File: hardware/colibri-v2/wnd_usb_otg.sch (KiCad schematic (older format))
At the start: 15 parts

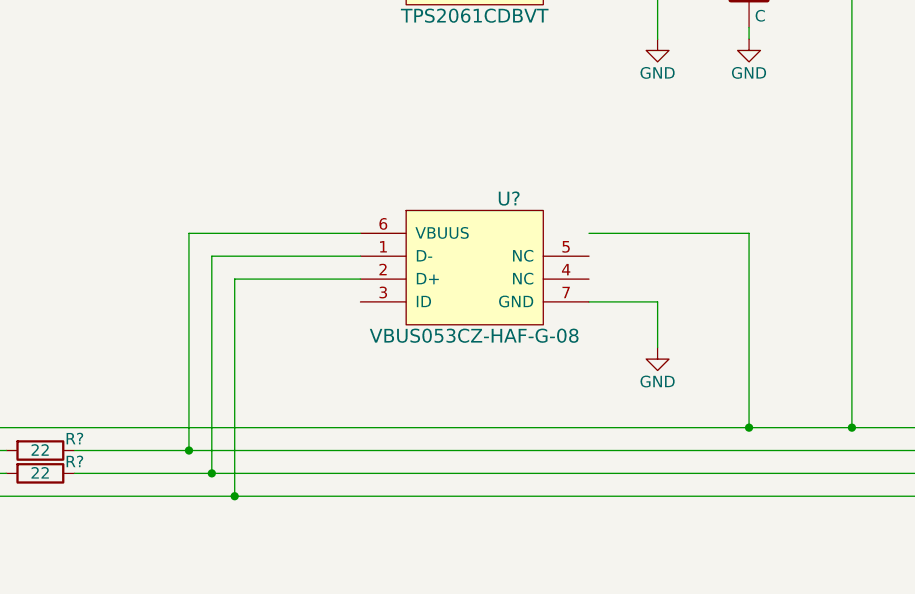
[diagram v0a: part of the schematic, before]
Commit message: Added Wandboard USB Host
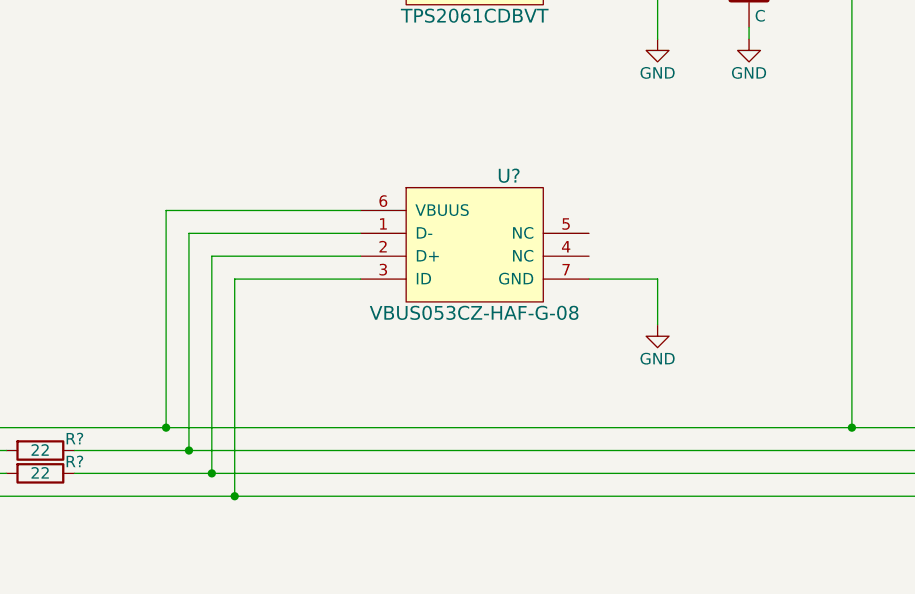
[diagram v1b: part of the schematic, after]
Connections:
- net OTG_FS_ID: now also U?.3 (ID); no longer U?.2 (D+)
- net VBUS_FS: now also U?.6 (VBUUS)
- net at P?.2 (D-), R?.1: now also U?.1 (D-); no longer U?.6 (VBUUS)
- net at P?.3 (D+), R?.1: now also U?.2 (D+); no longer U?.1 (D-)
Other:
- moved on the sheet: U?
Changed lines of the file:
@@
 $Descr A4 11693 8268
 encoding utf-8
-Sheet 13 21
+Sheet 13 22
 Title ""
 Date ""
@@
 L VBUS053CZ-HAF-G-08 U?
 U 1 1 5614C949
-P 4300 3850
-F 0 "U?" H 4450 4150 60  0000 C CNN
-F 1 "VBUS053CZ-HAF-G-08" H 4300 3550 60  0000 C CNN
-F 2 "" H 4250 4550 60  0000 C CNN
-F 3 "" H 4250 4550 60  0000 C CNN
-	1    4300 3850
+P 4300 3750
+F 0 "U?" H 4450 4050 60  0000 C CNN
+F 1 "VBUS053CZ-HAF-G-08" H 4300 3450 60  0000 C CNN
+F 2 "" H 4250 4450 60  0000 C CNN
+F 3 "" H 4250 4450 60  0000 C CNN
+	1    4300 3750
 	1    0    0    -1
 $EndComp
@@
 L GND #PWR?
 U 1 1 5614C9CE
-P 5100 4200
-F 0 "#PWR?" H 5100 3950 50  0001 C CNN
-F 1 "GND" H 5100 4050 50  0000 C CNN
-F 2 "" H 5100 4200 60  0000 C CNN
-F 3 "" H 5100 4200 60  0000 C CNN
-	1    5100 4200
+P 5100 4100
+F 0 "#PWR?" H 5100 3850 50  0001 C CNN
+F 1 "GND" H 5100 3950 50  0000 C CNN
+F 2 "" H 5100 4100 60  0000 C CNN
+F 3 "" H 5100 4100 60  0000 C CNN
+	1    5100 4100
 	1    0    0    -1
 $EndComp
@@
 Connection ~ 8100 2700
 Wire Wire Line
-	4800 4000 5100 4000
-Wire Wire Line
-	5100 4000 5100 4200
-Wire Wire Line
-	4800 3700 5500 3700
-Wire Wire Line
-	5500 3700 5500 4550
-Connection ~ 5500 4550
+	4800 3900 5100 3900
+Wire Wire Line
+	5100 3900 5100 4100
 Wire Wire Line
 	3800 3900 3250 3900
@@
 Wire Wire Line
 	5100 2600 5100 2850
+Wire Wire Line
+	3800 3600 2950 3600
+Wire Wire Line
+	2950 3600 2950 4550
+Connection ~ 2950 4550
 $EndSCHEMATC

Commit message: Annotated Components
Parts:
- gave numbers to parts that had none: 15
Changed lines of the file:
@@
 $EndDescr
 $Comp
-L USB_OTG P?
+L USB_OTG P8
 U 1 1 5614C935
 P 8300 4750
-F 0 "P?" H 8625 4625 50  0000 C CNN
+F 0 "P8" H 8625 4625 50  0000 C CNN
 F 1 "USB_OTG" H 8300 4950 50  0000 C CNN
 F 2 "" V 8250 4650 60  0000 C CNN
@@
 OTG_FS_PSO
 $Comp
-L VBUS053CZ-HAF-G-08 U?
+L VBUS053CZ-HAF-G-08 U10
 U 1 1 5614C949
 P 4300 3750
-F 0 "U?" H 4450 4050 60  0000 C CNN
+F 0 "U10" H 4450 4050 60  0000 C CNN
 F 1 "VBUS053CZ-HAF-G-08" H 4300 3450 60  0000 C CNN
 F 2 "" H 4250 4450 60  0000 C CNN
@@
 $EndComp
 $Comp
-L R R?
+L R R60
 U 1 1 5614C950
 P 2400 4650
-F 0 "R?" V 2350 4800 50  0000 C CNN
+F 0 "R60" V 2350 4800 50  0000 C CNN
 F 1 "22" V 2400 4650 50  0000 C CNN
 F 2 "" V 2330 4650 30  0000 C CNN
@@
 $EndComp
 $Comp
-L R R?
+L R R61
 U 1 1 5614C957
 P 2400 4750
-F 0 "R?" V 2350 4900 50  0000 C CNN
+F 0 "R61" V 2350 4900 50  0000 C CNN
 F 1 "22" V 2400 4750 50  0000 C CNN
 F 2 "" V 2330 4750 30  0000 C CNN
@@
 $EndComp
 $Comp
-L +3V3 #PWR?
+L +3V3 #PWR88
 U 1 1 5614C95E
 P 2100 1400
-F 0 "#PWR?" H 2100 1250 50  0001 C CNN
+F 0 "#PWR88" H 2100 1250 50  0001 C CNN
 F 1 "+3V3" H 2100 1540 50  0000 C CNN
 F 2 "" H 2100 1400 60  0000 C CNN
@@
 $EndComp
 $Comp
-L R R?
+L R R59
 U 1 1 5614C964
 P 2100 1950
-F 0 "R?" V 2180 1950 50  0000 C CNN
+F 0 "R59" V 2180 1950 50  0000 C CNN
 F 1 "10K" V 2100 1950 50  0000 C CNN
 F 2 "" V 2030 1950 30  0000 C CNN
@@
 $EndComp
 $Comp
-L +3V3 #PWR?
+L +3V3 #PWR89
 U 1 1 5614C96B
 P 2450 1400
-F 0 "#PWR?" H 2450 1250 50  0001 C CNN
+F 0 "#PWR89" H 2450 1250 50  0001 C CNN
 F 1 "+3V3" H 2450 1540 50  0000 C CNN
 F 2 "" H 2450 1400 60  0000 C CNN
@@
 $EndComp
 $Comp
-L R R?
+L R R62
 U 1 1 5614C971
 P 2450 1950
-F 0 "R?" V 2530 1950 50  0000 C CNN
+F 0 "R62" V 2530 1950 50  0000 C CNN
 F 1 "47K" V 2450 1950 50  0000 C CNN
 F 2 "" V 2380 1950 30  0000 C CNN
@@
 $EndComp
 $Comp
-L LED D?
+L LED D13
 U 1 1 5614C978
 P 2800 2100
-F 0 "D?" H 2800 2200 50  0000 C CNN
+F 0 "D13" H 2800 2200 50  0000 C CNN
 F 1 "RED" H 2800 2000 50  0000 C CNN
 F 2 "" H 2800 2100 60  0000 C CNN
@@
 $EndComp
 $Comp
-L R R?
+L R R63
 U 1 1 5614C97F
 P 2800 1650
-F 0 "R?" V 2880 1650 50  0000 C CNN
+F 0 "R63" V 2880 1650 50  0000 C CNN
 F 1 "620" V 2800 1650 50  0000 C CNN
 F 2 "" V 2730 1650 30  0000 C CNN
@@
 $EndComp
 $Comp
-L +3V3 #PWR?
+L +3V3 #PWR90
 U 1 1 5614C986
 P 2800 1400
-F 0 "#PWR?" H 2800 1250 50  0001 C CNN
+F 0 "#PWR90" H 2800 1250 50  0001 C CNN
 F 1 "+3V3" H 2800 1540 50  0000 C CNN
 F 2 "" H 2800 1400 60  0000 C CNN
@@
 $EndComp
 $Comp
-L LED D?
+L LED D14
 U 1 1 5614C98C
 P 8100 1850
-F 0 "D?" H 8100 1950 50  0000 C CNN
+F 0 "D14" H 8100 1950 50  0000 C CNN
 F 1 "GREEN" H 8100 1750 50  0000 C CNN
 F 2 "" H 8100 1850 60  0000 C CNN
@@
 $EndComp
 $Comp
-L R R?
+L R R66
 U 1 1 5614C993
 P 8100 1450
-F 0 "R?" V 8180 1450 50  0000 C CNN
+F 0 "R66" V 8180 1450 50  0000 C CNN
 F 1 "620" V 8100 1450 50  0000 C CNN
 F 2 "" V 8030 1450 30  0000 C CNN
@@
 $EndComp
 $Comp
-L +3V3 #PWR?
+L +3V3 #PWR96
 U 1 1 5614C99A
 P 8100 1200
-F 0 "#PWR?" H 8100 1050 50  0001 C CNN
+F 0 "#PWR96" H 8100 1050 50  0001 C CNN
 F 1 "+3V3" H 8100 1340 50  0000 C CNN
 F 2 "" H 8100 1200 60  0000 C CNN
@@
 $EndComp
 $Comp
-L Q_NMOS_GSD Q?
+L Q_NMOS_GSD Q7
 U 1 1 5614C9A0
 P 8000 2400
-F 0 "Q?" H 8300 2450 50  0000 R CNN
+F 0 "Q7" H 8300 2450 50  0000 R CNN
 F 1 "BSS138PW" H 8650 2350 50  0000 R CNN
 F 2 "" H 8200 2500 29  0000 C CNN
@@
 $EndComp
 $Comp
-L GND #PWR?
+L GND #PWR97
 U 1 1 5614C9A7
 P 8100 2850
-F 0 "#PWR?" H 8100 2600 50  0001 C CNN
+F 0 "#PWR97" H 8100 2600 50  0001 C CNN
 F 1 "GND" H 8100 2700 50  0000 C CNN
 F 2 "" H 8100 2850 60  0000 C CNN
@@
 $EndComp
 $Comp
-L R R?
+L R R64
 U 1 1 5614C9AD
 P 7300 2400
-F 0 "R?" V 7380 2400 50  0000 C CNN
+F 0 "R64" V 7380 2400 50  0000 C CNN
 F 1 "10K" V 7300 2400 50  0000 C CNN
 F 2 "" V 7230 2400 30  0000 C CNN
@@
 $EndComp
 $Comp
-L R R?
+L R R65
 U 1 1 5614C9B4
 P 7850 2700
-F 0 "R?" V 7930 2700 50  0000 C CNN
+F 0 "R65" V 7930 2700 50  0000 C CNN
 F 1 "47K" V 7850 2700 50  0000 C CNN
 F 2 "" V 7780 2700 30  0000 C CNN
@@
 $EndComp
 $Comp
-L C C?
+L C C64
 U 1 1 5614C9BB
 P 5500 2650
-F 0 "C?" H 5525 2750 50  0000 L CNN
+F 0 "C64" H 5525 2750 50  0000 L CNN
 F 1 "C" H 5525 2550 50  0000 L CNN
 F 2 "" H 5538 2500 30  0000 C CNN
@@
 $EndComp
 $Comp
-L GND #PWR?
+L GND #PWR94
 U 1 1 5614C9C2
 P 5500 2850
-F 0 "#PWR?" H 5500 2600 50  0001 C CNN
+F 0 "#PWR94" H 5500 2600 50  0001 C CNN
 F 1 "GND" H 5500 2700 50  0000 C CNN
 F 2 "" H 5500 2850 60  0000 C CNN
@@
 $EndComp
 $Comp
-L GND #PWR?
+L GND #PWR92
 U 1 1 5614C9C8
 P 5100 2850
-F 0 "#PWR?" H 5100 2600 50  0001 C CNN
+F 0 "#PWR92" H 5100 2600 50  0001 C CNN
 F 1 "GND" H 5100 2700 50  0000 C CNN
 F 2 "" H 5100 2850 60  0000 C CNN
@@
 $EndComp
 $Comp
-L GND #PWR?
+L GND #PWR93
 U 1 1 5614C9CE
 P 5100 4100
-F 0 "#PWR?" H 5100 3850 50  0001 C CNN
+F 0 "#PWR93" H 5100 3850 50  0001 C CNN
 F 1 "GND" H 5100 3950 50  0000 C CNN
 F 2 "" H 5100 4100 60  0000 C CNN
@@
 Connection ~ 3050 4650
 $Comp
-L GND #PWR?
+L GND #PWR95
 U 1 1 5614CA07
 P 7900 5400
-F 0 "#PWR?" H 7900 5150 50  0001 C CNN
+F 0 "#PWR95" H 7900 5150 50  0001 C CNN
 F 1 "GND" H 7900 5250 50  0000 C CNN
 F 2 "" H 7900 5400 60  0000 C CNN
@@
 Connection ~ 7900 5300
 $Comp
-L +5V #PWR?
+L +5V #PWR91
 U 1 1 5614CA12
 P 3150 1400
-F 0 "#PWR?" H 3150 1250 50  0001 C CNN
+F 0 "#PWR91" H 3150 1250 50  0001 C CNN
 F 1 "+5V" H 3150 1540 50  0000 C CNN
 F 2 "" H 3150 1400 60  0000 C CNN
@@
 $EndComp
 $Comp
-L TPS2061CDBVT U?
+L TPS2061CDBVT U9
 U 1 1 5614D158
 P 4300 2500
-F 0 "U?" H 4550 2750 60  0000 C CNN
+F 0 "U9" H 4550 2750 60  0000 C CNN
 F 1 "TPS2061CDBVT" H 4300 2250 60  0000 C CNN
 F 2 "" H 4300 2300 60  0000 C CNN

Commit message: Re-annotated schematic
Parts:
- renumbered C64 to C62, R59 to R60, R60 to R61, R61 to R62, R62 to R63, R63 to R64, R64 to R65, R65 to R66, R66 to R67
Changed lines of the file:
@@
 $EndComp
 $Comp
-L R R60
+L R R61
 U 1 1 5614C950
 P 2400 4650
-F 0 "R60" V 2350 4800 50  0000 C CNN
+F 0 "R61" V 2350 4800 50  0000 C CNN
 F 1 "22" V 2400 4650 50  0000 C CNN
 F 2 "" V 2330 4650 30  0000 C CNN
@@
 $EndComp
 $Comp
-L R R61
+L R R62
 U 1 1 5614C957
 P 2400 4750
-F 0 "R61" V 2350 4900 50  0000 C CNN
+F 0 "R62" V 2350 4900 50  0000 C CNN
 F 1 "22" V 2400 4750 50  0000 C CNN
 F 2 "" V 2330 4750 30  0000 C CNN
@@
 $EndComp
 $Comp
-L +3V3 #PWR090
+L +3V3 #PWR85
 U 1 1 5614C95E
 P 2100 1400
-F 0 "#PWR090" H 2100 1250 50  0001 C CNN
+F 0 "#PWR85" H 2100 1250 50  0001 C CNN
 F 1 "+3V3" H 2100 1540 50  0000 C CNN
 F 2 "" H 2100 1400 60  0000 C CNN
@@
 $EndComp
 $Comp
-L R R59
+L R R60
 U 1 1 5614C964
 P 2100 1950
-F 0 "R59" V 2180 1950 50  0000 C CNN
+F 0 "R60" V 2180 1950 50  0000 C CNN
 F 1 "10K" V 2100 1950 50  0000 C CNN
 F 2 "" V 2030 1950 30  0000 C CNN
@@
 $EndComp
 $Comp
-L +3V3 #PWR091
+L +3V3 #PWR86
 U 1 1 5614C96B
 P 2450 1400
-F 0 "#PWR091" H 2450 1250 50  0001 C CNN
+F 0 "#PWR86" H 2450 1250 50  0001 C CNN
 F 1 "+3V3" H 2450 1540 50  0000 C CNN
 F 2 "" H 2450 1400 60  0000 C CNN
@@
 $EndComp
 $Comp
-L R R62
+L R R63
 U 1 1 5614C971
 P 2450 1950
-F 0 "R62" V 2530 1950 50  0000 C CNN
+F 0 "R63" V 2530 1950 50  0000 C CNN
 F 1 "47K" V 2450 1950 50  0000 C CNN
 F 2 "" V 2380 1950 30  0000 C CNN
@@
 $EndComp
 $Comp
-L R R63
+L R R64
 U 1 1 5614C97F
 P 2800 1650
-F 0 "R63" V 2880 1650 50  0000 C CNN
+F 0 "R64" V 2880 1650 50  0000 C CNN
 F 1 "620" V 2800 1650 50  0000 C CNN
 F 2 "" V 2730 1650 30  0000 C CNN
@@
 $EndComp
 $Comp
-L +3V3 #PWR092
+L +3V3 #PWR87
 U 1 1 5614C986
 P 2800 1400
-F 0 "#PWR092" H 2800 1250 50  0001 C CNN
+F 0 "#PWR87" H 2800 1250 50  0001 C CNN
 F 1 "+3V3" H 2800 1540 50  0000 C CNN
 F 2 "" H 2800 1400 60  0000 C CNN
@@
 $EndComp
 $Comp
-L R R66
+L R R67
 U 1 1 5614C993
 P 8100 1450
-F 0 "R66" V 8180 1450 50  0000 C CNN
+F 0 "R67" V 8180 1450 50  0000 C CNN
 F 1 "620" V 8100 1450 50  0000 C CNN
 F 2 "" V 8030 1450 30  0000 C CNN
@@
 $EndComp
 $Comp
-L +3V3 #PWR093
+L +3V3 #PWR93
 U 1 1 5614C99A
 P 8100 1200
-F 0 "#PWR093" H 8100 1050 50  0001 C CNN
+F 0 "#PWR93" H 8100 1050 50  0001 C CNN
 F 1 "+3V3" H 8100 1340 50  0000 C CNN
 F 2 "" H 8100 1200 60  0000 C CNN
@@
 $EndComp
 $Comp
-L GND #PWR094
+L GND #PWR94
 U 1 1 5614C9A7
 P 8100 2850
-F 0 "#PWR094" H 8100 2600 50  0001 C CNN
+F 0 "#PWR94" H 8100 2600 50  0001 C CNN
 F 1 "GND" H 8100 2700 50  0000 C CNN
 F 2 "" H 8100 2850 60  0000 C CNN
@@
 $EndComp
 $Comp
-L R R64
+L R R65
 U 1 1 5614C9AD
 P 7300 2400
-F 0 "R64" V 7380 2400 50  0000 C CNN
+F 0 "R65" V 7380 2400 50  0000 C CNN
 F 1 "10K" V 7300 2400 50  0000 C CNN
 F 2 "" V 7230 2400 30  0000 C CNN
@@
 $EndComp
 $Comp
-L R R65
+L R R66
 U 1 1 5614C9B4
 P 7850 2700
-F 0 "R65" V 7930 2700 50  0000 C CNN
+F 0 "R66" V 7930 2700 50  0000 C CNN
 F 1 "47K" V 7850 2700 50  0000 C CNN
 F 2 "" V 7780 2700 30  0000 C CNN
@@
 $EndComp
 $Comp
-L C C64
+L C C62
 U 1 1 5614C9BB
 P 5500 2650
-F 0 "C64" H 5525 2750 50  0000 L CNN
+F 0 "C62" H 5525 2750 50  0000 L CNN
 F 1 "C" H 5525 2550 50  0000 L CNN
 F 2 "" H 5538 2500 30  0000 C CNN
@@
 $EndComp
 $Comp
-L GND #PWR095
+L GND #PWR91
 U 1 1 5614C9C2
 P 5500 2850
-F 0 "#PWR095" H 5500 2600 50  0001 C CNN
+F 0 "#PWR91" H 5500 2600 50  0001 C CNN
 F 1 "GND" H 5500 2700 50  0000 C CNN
 F 2 "" H 5500 2850 60  0000 C CNN
@@
 $EndComp
 $Comp
-L GND #PWR096
+L GND #PWR89
 U 1 1 5614C9C8
 P 5100 2850
-F 0 "#PWR096" H 5100 2600 50  0001 C CNN
+F 0 "#PWR89" H 5100 2600 50  0001 C CNN
 F 1 "GND" H 5100 2700 50  0000 C CNN
 F 2 "" H 5100 2850 60  0000 C CNN
@@
 $EndComp
 $Comp
-L GND #PWR097
+L GND #PWR90
 U 1 1 5614C9CE
 P 5100 4100
-F 0 "#PWR097" H 5100 3850 50  0001 C CNN
+F 0 "#PWR90" H 5100 3850 50  0001 C CNN
 F 1 "GND" H 5100 3950 50  0000 C CNN
 F 2 "" H 5100 4100 60  0000 C CNN
@@
 Connection ~ 3050 4650
 $Comp
-L GND #PWR098
+L GND #PWR92
 U 1 1 5614CA07
 P 7900 5400
-F 0 "#PWR098" H 7900 5150 50  0001 C CNN
+F 0 "#PWR92" H 7900 5150 50  0001 C CNN
 F 1 "GND" H 7900 5250 50  0000 C CNN
 F 2 "" H 7900 5400 60  0000 C CNN
@@
 Connection ~ 7900 5300
 $Comp
-L +5V #PWR099
+L +5V #PWR88
 U 1 1 5614CA12
 P 3150 1400
-F 0 "#PWR099" H 3150 1250 50  0001 C CNN
+F 0 "#PWR88" H 3150 1250 50  0001 C CNN
 F 1 "+5V" H 3150 1540 50  0000 C CNN
 F 2 "" H 3150 1400 60  0000 C CNN

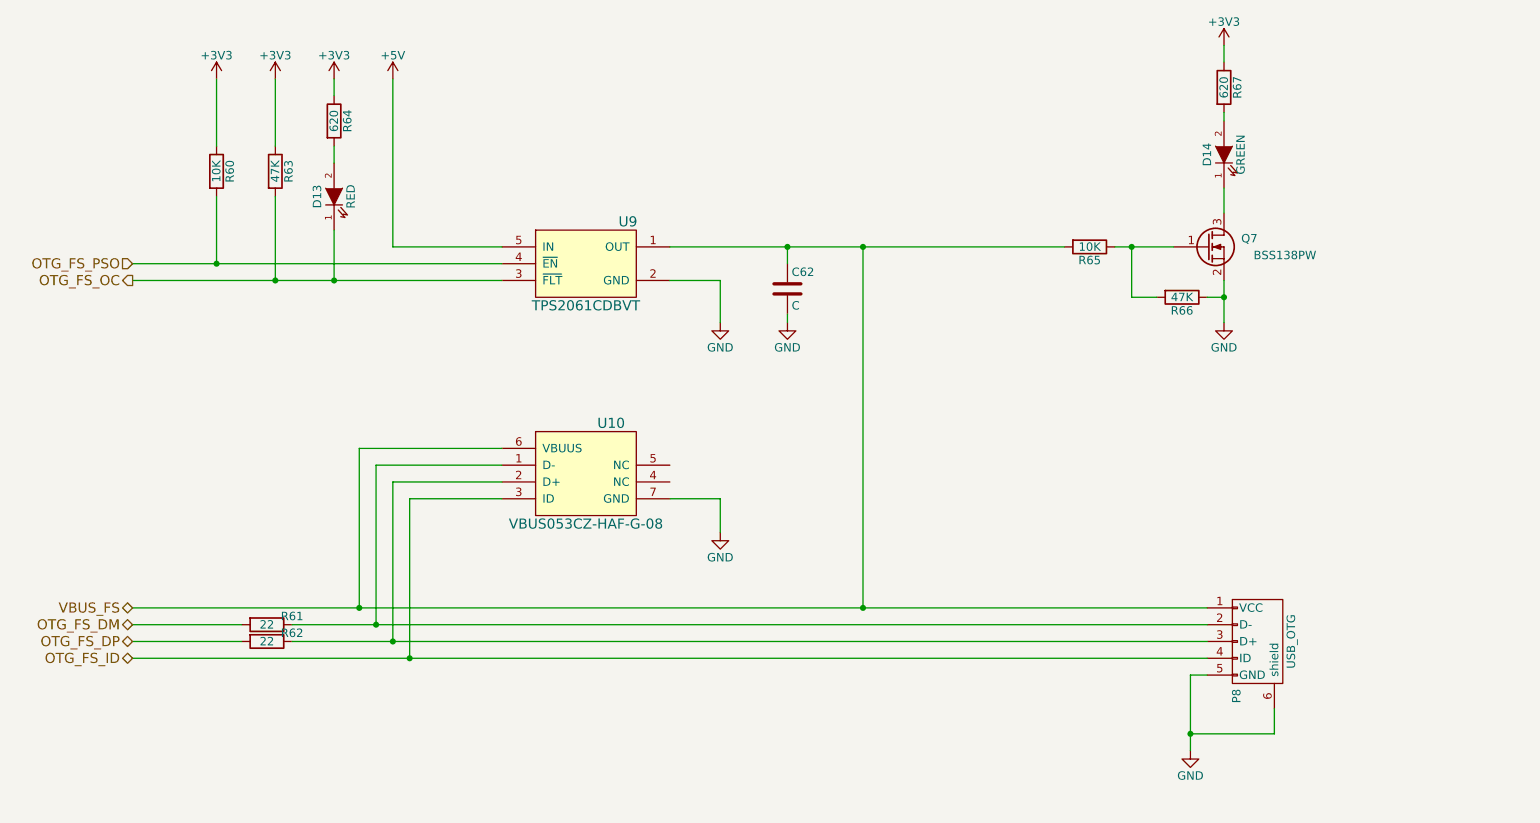
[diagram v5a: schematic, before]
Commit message: Associated footprints for R and some of the C
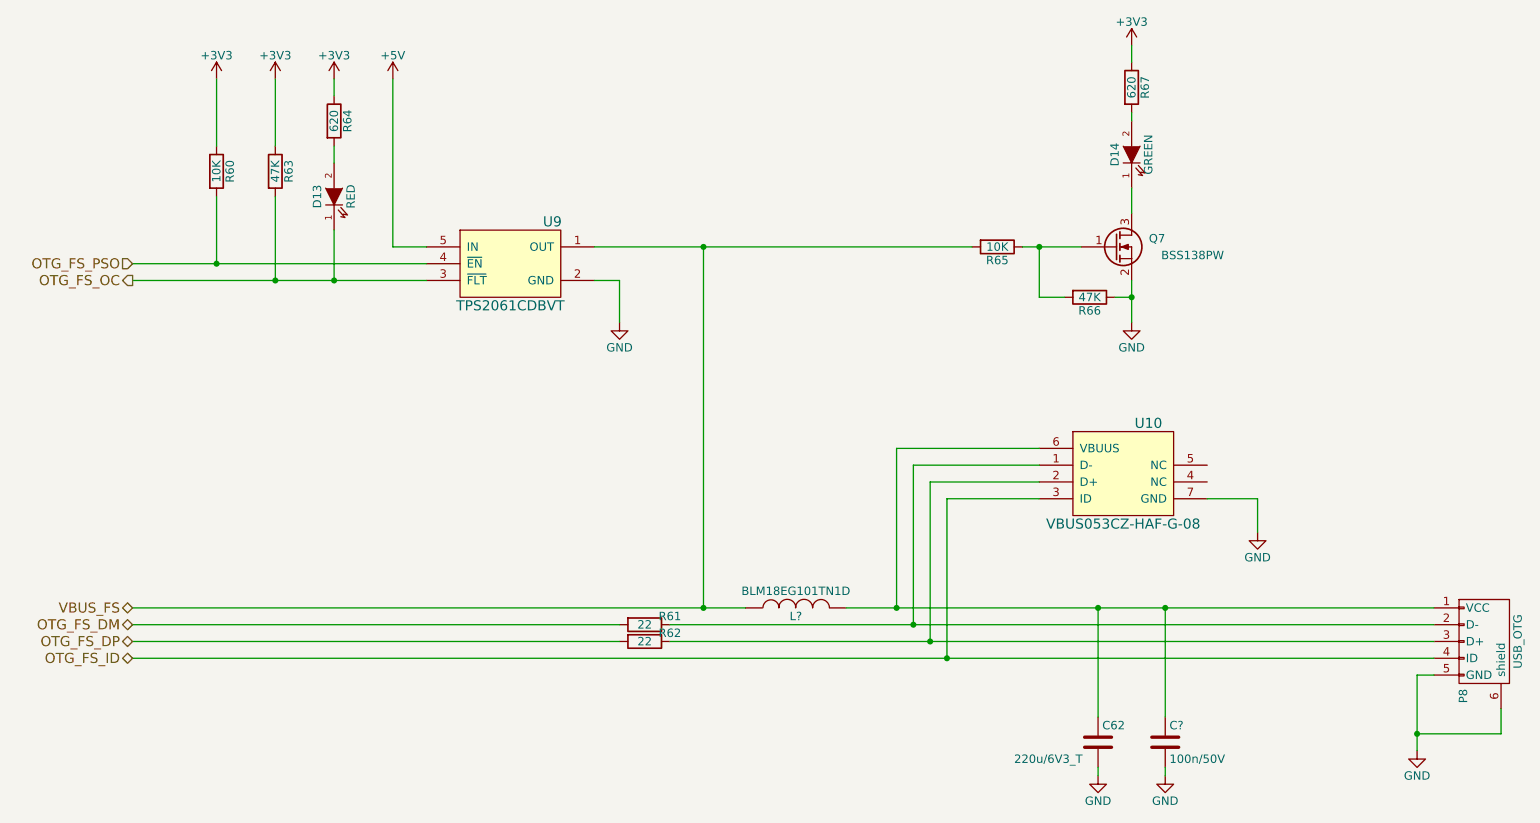
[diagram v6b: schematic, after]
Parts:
- added C?: 100n/50V, symbol C
- added L?: BLM18EG101TN1D, symbol INDUCTOR
- C62: value C -> 220u/6V3_T
- R60, R61, R62, R63, R64, R65, R66, R67: footprint (none) -> Resistors_SMD:R_0603
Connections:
- net GND: now also C?.2
- net VBUS_FS: now also L?.1; no longer C62.1, P8.1 (VCC), U10.6 (VBUUS)
- new net: C62.1, C?.1, L?.2, P8.1 (VCC), U10.6 (VBUUS)
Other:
- moved on the sheet: C62, D14, P8, Q7, R61, R62, R65, R66, R67, U10, U9
